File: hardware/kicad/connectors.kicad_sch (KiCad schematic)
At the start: 0 parts

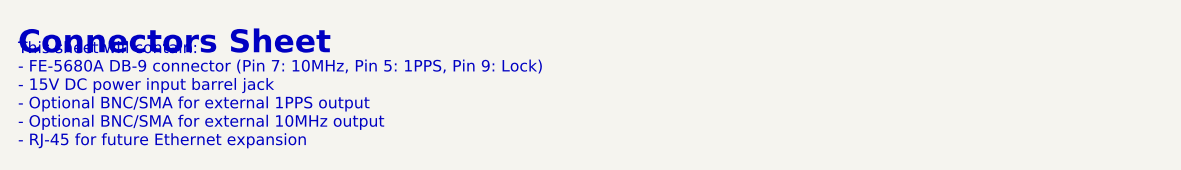
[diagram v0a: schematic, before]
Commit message: Update FE-5680A pinout and add NPN level shifter for lock detection
- Correct DB-9 pinout: Pin 1 (+15V), Pin 2 (GND), Pin 3 (Lock),
  Pin 4 (+5V), Pin 5 (GND), Pin 7 (10MHz)
- Add NPN transistor (2N3904) level shifter circuit for lock status:
  22k input resistor, 10k base-to-GND, 10k collector pull-up
- FE-5680A outputs 4.8V (unlocked) / 0.8V (locked)
- Transistor inverts signal: GPIO HIGH = locked, LOW = unlocked
- Update firmware to remove signal inversion in check_rb_lock()
- Remove internal pull-up (external pull-up via collector resistor)
- Update all documentation and schematics

🤖 Generated with [Claude Code](https://claude.com/claude-code)

Co-Authored-By: Claude Opus 4.5 <noreply@anthropic.com>
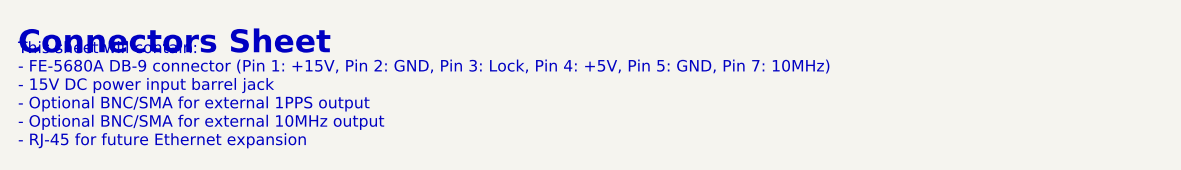
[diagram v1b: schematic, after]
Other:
- note added: "This sheet will contain: - FE-5680A DB-9 connector (Pin 1: +15V, Pin 2: GND, Pin 3: Lock, Pin 4: +5V, Pin 5: GND, Pin 7: 10MHz) - 15V DC power input barrel jack - Optional BNC/SMA for external 1PPS output - Optional BNC/SMA for external 10MHz output - RJ-45 for future Ethernet expansion"
- note removed: "This sheet will contain: - FE-5680A DB-9 connector (Pin 7: 10MHz, Pin 5: 1PPS, Pin 9: Lock) - 15V DC power input barrel jack - Optional BNC/SMA for external 1PPS output - Optional BNC/SMA for external 10MHz output - RJ-45 for future Ethernet expansion"
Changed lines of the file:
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@@
 		)
 	)
-	(text "This sheet will contain:\n- FE-5680A DB-9 connector (Pin 7: 10MHz, Pin 5: 1PPS, Pin 9: Lock)\n- 15V DC power input barrel jack\n- Optional BNC/SMA for external 1PPS output\n- Optional BNC/SMA for external 10MHz output\n- RJ-45 for future Ethernet expansion"
+	(text "This sheet will contain:\n- FE-5680A DB-9 connector (Pin 1: +15V, Pin 2: GND, Pin 3: Lock, Pin 4: +5V, Pin 5: GND, Pin 7: 10MHz)\n- 15V DC power input barrel jack\n- Optional BNC/SMA for external 1PPS output\n- Optional BNC/SMA for external 10MHz output\n- RJ-45 for future Ethernet expansion"
 		(exclude_from_sim no)
 		(at 50.8 60.96 0)
